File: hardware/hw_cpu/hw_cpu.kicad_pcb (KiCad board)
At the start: 2 copper layers, 89.5 x 59.7 mm, 70 parts, among them J1 CON_EXT, J2 Micro_SD_Card_Det, J3 SDIO_DEB, J4 PROG, SW1 RUN/STOP, SW2 RESTORE, SW3 DUMP, SW4 RESET, U1 STM32F429ZGTx, U2 MT48LC4M16A2P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

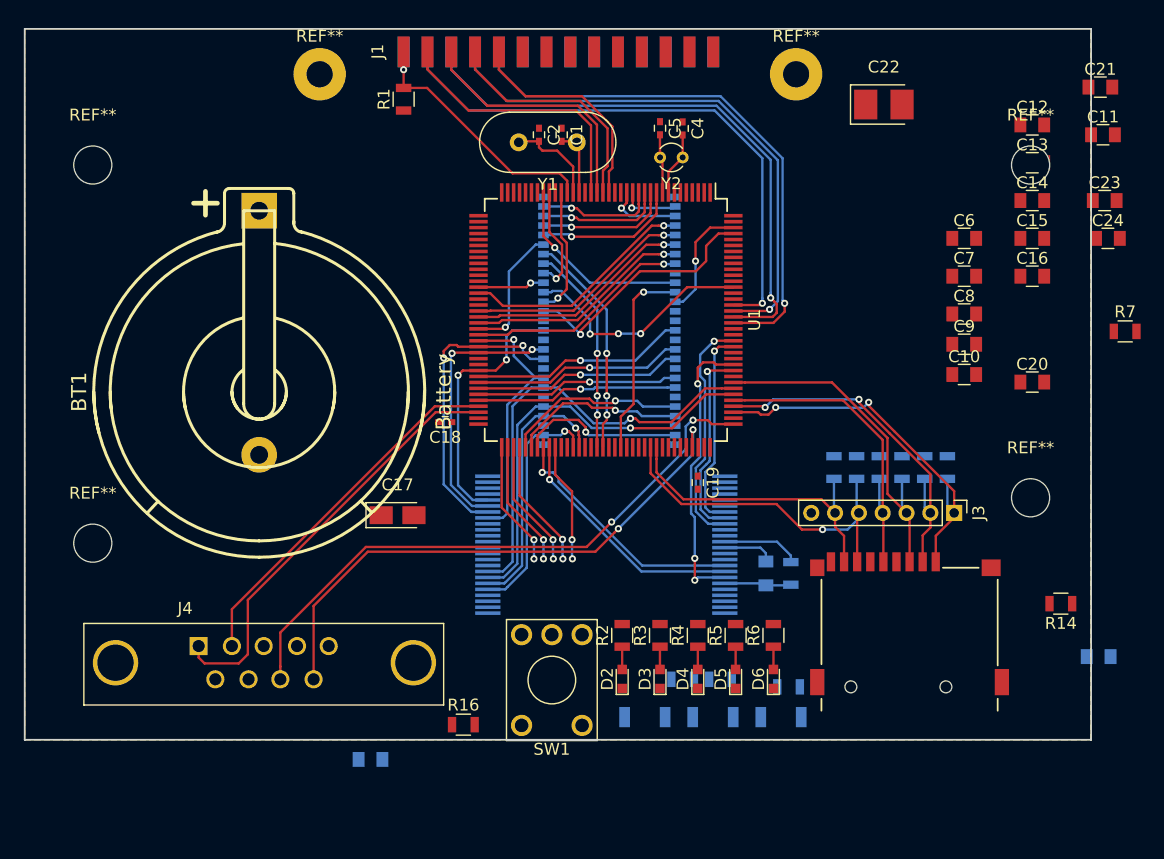
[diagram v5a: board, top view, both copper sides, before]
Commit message: Обновлена плата CPU.
Завершена предварительная трассировка
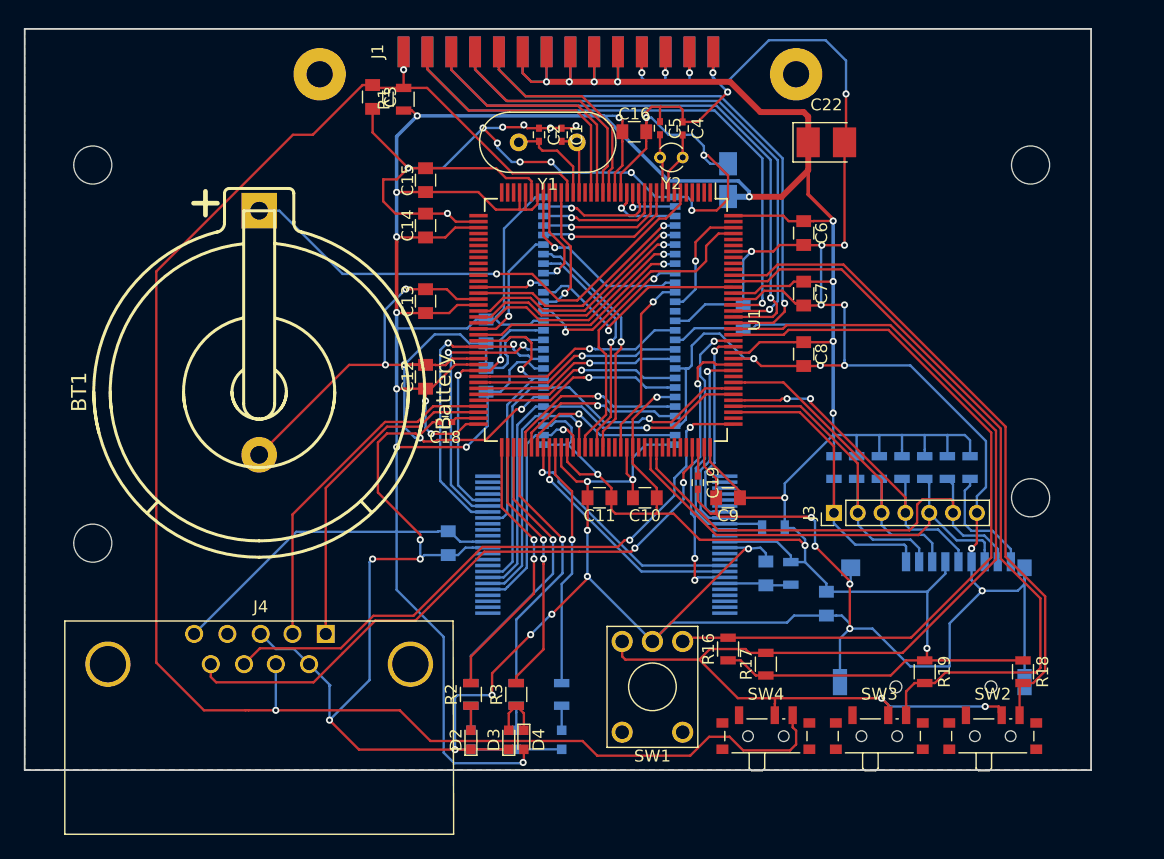
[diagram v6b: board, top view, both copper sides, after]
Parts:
- added D7: CFL, LEDs:LED_0603, B.Cu at (99.7, 130.8)
- C17, C20, C21, C23, C24, J2, R14, R4, R5, R6, R7: moved to B.Cu
- C3, R17, R18, R19: moved to F.Cu
- D2: value LED -> PWR
- D3: value LED -> RUN
- D4: value LED -> STOP
- D5: value LED -> ERR; moved to B.Cu
- D6: value LED -> FLT; moved to B.Cu
- J4: footprint Connect:DB9MD -> Connect:DB9FC
- SW2, SW3, SW4: footprint Buttons_Switches_SMD:SW_SPST_B3U-3000P -> Buttons_Switches_SMD:SW_SPDT_PCM12; moved to F.Cu
- U2: value MT48LC4M16A2P -> MT48LC32M16A2P
- moved C21 66.8 mm to (90.2, 114.3), turned to 270 degrees
- moved C3 55.6 mm to (83.8, 76.8), turned to 270 degrees
- moved C12 55.2 mm to (88.3, 100.3), turned to 90 degrees
- moved C23 53.1 mm to (93.3, 96.5), turned to 270 degrees
- moved C13 52.3 mm to (88.3, 94.0), turned to 90 degrees
- moved C11 52.1 mm to (102.9, 110.5), turned to 180 degrees
- moved C15 51.2 mm to (88.3, 83.8), turned to 90 degrees
- moved C14 51.0 mm to (88.3, 87.6), turned to 90 degrees
- moved C20 45.9 mm to (93.3, 100.6), turned to 90 degrees
- moved C17 39.5 mm to (113.7, 83.8), turned to 90 degrees
- moved C16 35.5 mm to (105.8, 79.8)
- moved R7 33.8 mm to (117.5, 113.0)
- moved C24 31.3 mm to (114.9, 95.2), turned to 90 degrees
- moved C10 28.7 mm to (106.7, 110.5), turned to 180 degrees
- moved C9 23.6 mm to (113.7, 110.5), turned to 180 degrees
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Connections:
- D4 pad 1: BOOT0 -> Net-(D3-Pad2)
- D4 pad 2: Net-(D4-Pad2) -> VREF
- J2 pad 9: BOOT0 -> CARD_DET
- R4 pad 1: Net-(D4-Pad2) -> Net-(D5-Pad2)
- R5 pad 1: Net-(D5-Pad2) -> Net-(D6-Pad2)
- R6 pad 1: Net-(D6-Pad2) -> Net-(D7-Pad2)
- SW2 pad 1: STOP -> Net-(SW2-Pad1)
- SW2 pad 2: FW_REST -> STOP
- SW3 pad 1: STOP -> Net-(SW3-Pad1)
- SW3 pad 2: FW_DUMP -> STOP
- SW4 pad 1: STOP -> Net-(SW4-Pad1)
- SW4 pad 2: RESET -> STOP
- U1 pad 124: Net-(U1-Pad124) -> RUN
- U1 pad 125: Net-(U1-Pad125) -> STOP
- U1 pad 133: Net-(U1-Pad133) -> FW_DUMP
- U1 pad 134: Net-(U1-Pad134) -> FW_REST
- U2 pad 36: (no net) -> A12
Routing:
- net BOOT0: track 4.34 -> 563.3 mm, vias 0 -> 52
- net VREF: track 6.58 -> 498.5 mm, vias 0 -> 25
- net RESET: track 22.5 -> 147.4 mm, vias 1 -> 2
- net STOP: track 0.00 -> 103.9 mm, vias 0 -> 2
- net RUN: track 0.00 -> 64.7 mm
- net FW_DUMP: track 0.00 -> 64.0 mm
- net FW_REST: track 0.00 -> 55.9 mm
- net VBAT: track 0.00 -> 42.8 mm, vias 0 -> 1
- net A12: track 0.00 -> 19.2 mm, vias 0 -> 1
- net SDIO_D1: track 25.8 -> 41.6 mm
- net LED3: track 10.7 -> 24.0 mm, vias 2 -> 1
- net LED1: track 10.5 -> 23.1 mm
- net LED4: track 10.9 -> 22.9 mm, vias 2 -> 1
- net LED2: track 10.6 -> 22.0 mm
- net LED5: track 9.96 -> 20.7 mm, vias 2 -> 1
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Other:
- board size 89.5 x 59.7 mm -> 89.5 x 62.2 mm
